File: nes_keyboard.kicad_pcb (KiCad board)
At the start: 2 copper layers, 323.9 x 115.5 mm, 257 parts, among them J1 USB_C_Receptacle_USB2.0_16P, SW1 SW_Push, SW2 SW_Push, SW3 RotaryEncoder_Switch_MP, U1 RP2040, U2 NCP1117-3.3_SOT223, U3 W25Q128JVE, U4 74AHCT1G125, Y1 Crystal_GND24

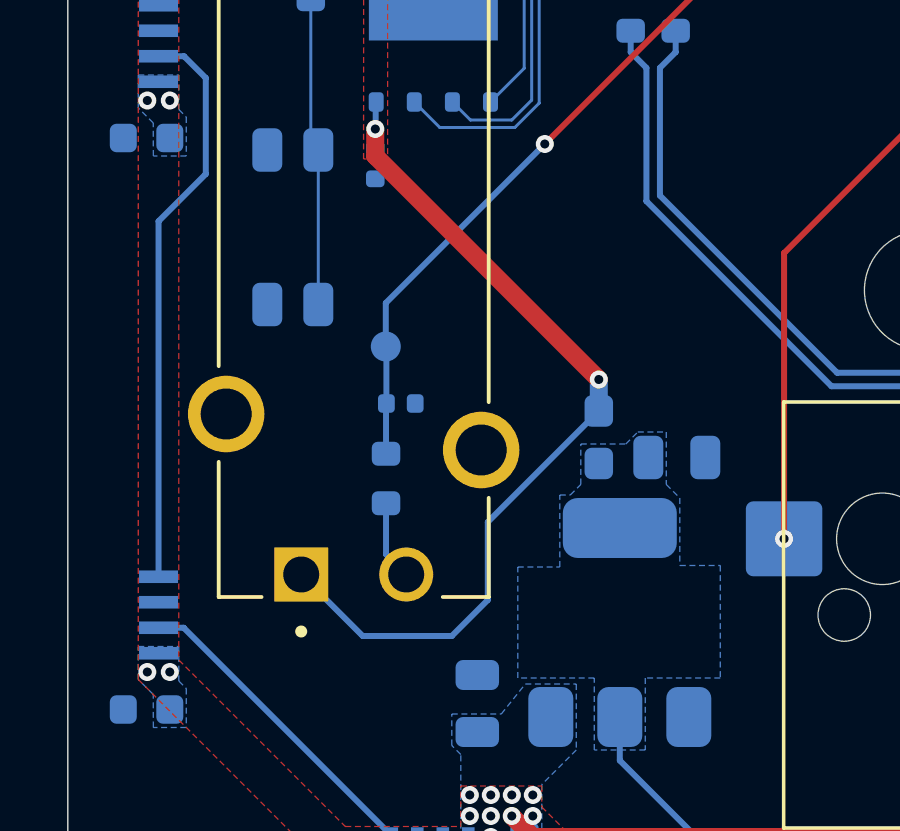
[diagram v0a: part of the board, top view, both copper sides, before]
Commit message: Added switchplate - V0.4
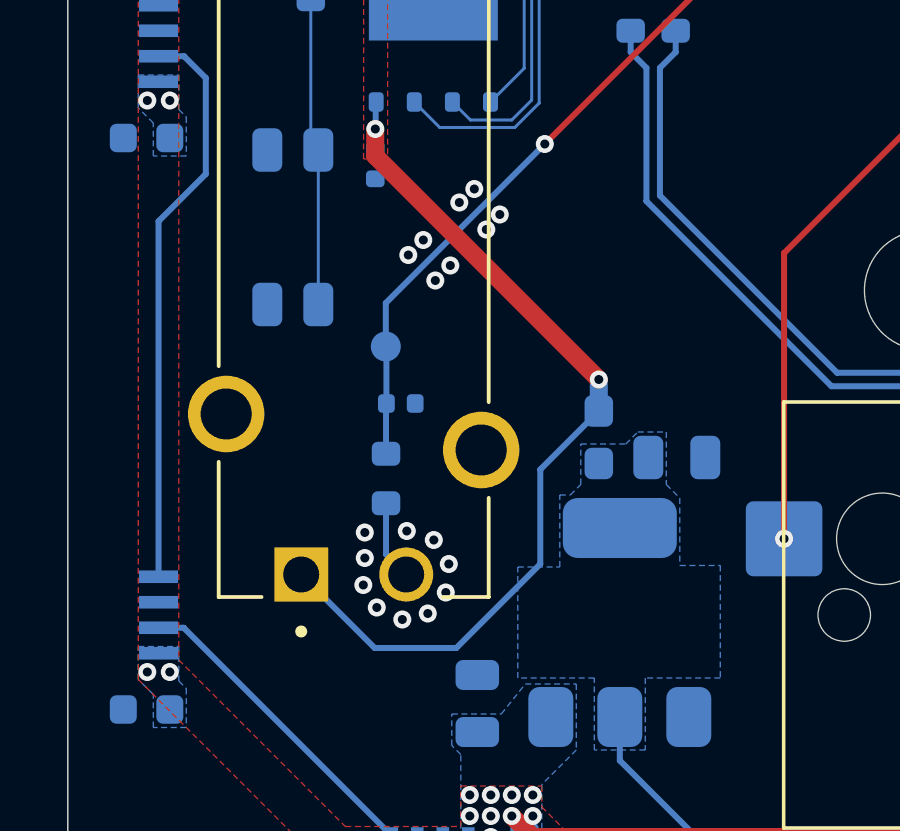
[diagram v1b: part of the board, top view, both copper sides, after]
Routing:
- net +3V3: track 165.7 -> 166.3 mm
- net GND: vias 13 -> 31
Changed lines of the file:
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@@
-	)
-	(segment
-		(start 64 134.65)
-		(end 67.7 130.95)
-		(width 0.2)
-		(layer "B.Cu")
-		(net "+3V3")
 	)
 	(segment
@@
 	)
 	(segment
-		(start 62.8 138.45)
-		(end 64 137.25)
-		(width 0.2)
-		(layer "B.Cu")
-		(net "+3V3")
-	)
-	(segment
 		(start 67.55 104.2)
 		(end 68.5125 103.2375)
@@
 	)
 	(segment
+		(start 62.95 138.85)
+		(end 65.75 136.05)
+		(width 0.2)
+		(layer "B.Cu")
+		(net "+3V3")
+	)
+	(segment
 		(start 68.9125 109.1875)
 		(end 69.2625 108.8375)
@@
 	)
 	(segment
-		(start 59.83 138.45)
-		(end 62.8 138.45)
+		(start 65.75 136.05)
+		(end 65.75 132.9)
 		(width 0.2)
 		(layer "B.Cu")
@@
 	)
 	(segment
+		(start 57.78 136.4)
+		(end 60.23 138.85)
+		(width 0.2)
+		(layer "B.Cu")
+		(net "+3V3")
+	)
+	(segment
 		(start 55.355 40)
 		(end 56.2 40)
@@
 	)
 	(segment
+		(start 60.23 138.85)
+		(end 62.95 138.85)
+		(width 0.2)
+		(layer "B.Cu")
+		(net "+3V3")
+	)
+	(segment
 		(start 68.9125 110.4375)
 		(end 68.9125 109.675)
@@
 	)
 	(segment
-		(start 57.78 136.4)
-		(end 59.83 138.45)
+		(start 65.75 132.9)
+		(end 67.7 130.95)
 		(width 0.2)
 		(layer "B.Cu")
@@
 	)
 	(segment
-		(start 64 137.25)
-		(end 64 134.65)
-		(width 0.2)
-		(layer "B.Cu")
-		(net "+3V3")
-	)
-	(segment
 		(start 68.9125 109.675)
 		(end 68.9125 109.1875)
@@
 	)
 	(via
+		(at 61.3 134.95)
+		(size 0.6)
+		(drill 0.3)
+		(layers "F.Cu" "B.Cu")
+		(free yes)
+		(net "GND")
+	)
+	(via
+		(at 62.7 136.05)
+		(size 0.6)
+		(drill 0.3)
+		(layers "F.Cu" "B.Cu")
+		(free yes)
+		(net "GND")
+	)
+	(via
+		(at 59.9 135)
+		(size 0.6)
+		(drill 0.3)
+		(layers "F.Cu" "B.Cu")
+		(free yes)
+		(net "GND")
+	)
+	(via
 		(at 62.65 110.5)
 		(size 0.6)
@@
 	)
 	(via
+		(at 62.25 126.6)
+		(size 0.6)
+		(drill 0.3)
+		(layers "F.Cu" "B.Cu")
+		(free yes)
+		(net "GND")
+	)
+	(via
 		(at 62.185 116.9)
 		(size 0.6)
@@
 	)
 	(via
+		(at 61.15 137.9)
+		(size 0.6)
+		(drill 0.3)
+		(layers "F.Cu" "B.Cu")
+		(free yes)
+		(net "GND")
+	)
+	(via
 		(at 60.9 102.85)
 		(size 0.6)
@@
 	)
 	(via
+		(at 60.3 137.5)
+		(size 0.6)
+		(drill 0.3)
+		(layers "F.Cu" "B.Cu")
+		(free yes)
+		(net "GND")
+	)
+	(via
 		(at 67.25 114.1)
 		(size 0.6)
@@
 	)
 	(via
+		(at 62.6 137)
+		(size 0.6)
+		(drill 0.3)
+		(layers "F.Cu" "B.Cu")
+		(free yes)
+		(net "GND")
+	)
+	(via
+		(at 63.95 124.9)
+		(size 0.6)
+		(drill 0.3)
+		(layers "F.Cu" "B.Cu")
+		(free yes)
+		(net "GND")
+	)
+	(via
+		(at 59.9 135.85)
+		(size 0.6)
+		(drill 0.3)
+		(layers "F.Cu" "B.Cu")
+		(free yes)
+		(net "GND")
+	)
+	(via
 		(at 75.8 109)
 		(size 0.6)
@@
 	)
 	(via
+		(at 61.85 125.25)
+		(size 0.6)
+		(drill 0.3)
+		(layers "F.Cu" "B.Cu")
+		(free yes)
+		(net "GND")
+	)
+	(via
+		(at 61.35 125.75)
+		(size 0.6)
+		(drill 0.3)
+		(layers "F.Cu" "B.Cu")
+		(free yes)
+		(net "GND")
+	)
+	(via
 		(at 60.05 102)
 		(size 0.6)
@@
 	)
 	(via
+		(at 64.4 124.4)
+		(size 0.6)
+		(drill 0.3)
+		(layers "F.Cu" "B.Cu")
+		(free yes)
+		(net "GND")
+	)
+	(via
+		(at 62.75 126.1)
+		(size 0.6)
+		(drill 0.3)
+		(layers "F.Cu" "B.Cu")
+		(free yes)
+		(net "GND")
+	)
+	(via
+		(at 62 137.7)
+		(size 0.6)
+		(drill 0.3)
+		(layers "F.Cu" "B.Cu")
+		(free yes)
+		(net "GND")
+	)
+	(via
 		(at 75.7 103.7)
 		(size 0.6)
@@
 	)
 	(via
+		(at 62.2 135.25)
+		(size 0.6)
+		(drill 0.3)
+		(layers "F.Cu" "B.Cu")
+		(free yes)
+		(net "GND")
+	)
+	(via
 		(at 69.2875 94.8375)
 		(size 0.6)
 		(drill 0.3)
+		(layers "F.Cu" "B.Cu")
+		(free yes)
+		(net "GND")
+	)
+	(via
+		(at 63.55 123.55)
+		(size 0.6)
+		(drill 0.3)
+		(layers "F.Cu" "B.Cu")
+		(free yes)
+		(net "GND")
+	)
+	(via
+		(at 63.05 124)
+		(size 0.6)
+		(drill 0.3)
+		(layers "F.Cu" "B.Cu")
+		(free yes)
+		(net "GND")
+	)
+	(via
+		(at 59.85 136.75)
+		(size 0.6)
+		(drill 0.3)
